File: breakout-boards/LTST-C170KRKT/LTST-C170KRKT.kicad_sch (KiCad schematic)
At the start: 0 parts

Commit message: feat: add red LED breakout board
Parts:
- added J1, J2: Conn_01x12, Connector_PinSocket_2.54mm:PinSocket_1x12_P2.54mm_Vertical, symbol Connector_Generic:Conn_01x12
- added LED1, LED10, LED11, LED12, LED2, LED3, LED4, LED5, LED6, LED7, LED8, LED9: LTST-C170KRKT, LEDC2012X120N, symbol FixedWing:LTST-C170KRKT
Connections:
- new net: J1.10 (Pin_10), LED3.1 (K)
- new net: J2.10 (Pin_10), LED3.2 (A)
- new net: J1.7 (Pin_7), LED6.1 (K)
- new net: J2.7 (Pin_7), LED6.2 (A)
- new net: J1.4 (Pin_4), LED9.1 (K)
- new net: J2.4 (Pin_4), LED9.2 (A)
- new net: J1.1 (Pin_1), LED12.1 (K)
- new net: J2.1 (Pin_1), LED12.2 (A)
- new net: J1.9 (Pin_9), LED4.1 (K)
- new net: J2.9 (Pin_9), LED4.2 (A)
- new net: J1.11 (Pin_11), LED2.1 (K)
- new net: J1.12 (Pin_12), LED1.1 (K)
- new net: J1.2 (Pin_2), LED11.1 (K)
- new net: J1.3 (Pin_3), LED10.1 (K)
- new net: J1.5 (Pin_5), LED8.1 (K)
- new net: J1.6 (Pin_6), LED7.1 (K)
- new net: J1.8 (Pin_8), LED5.1 (K)
- new net: J2.12 (Pin_12), LED1.2 (A)
- new net: J2.8 (Pin_8), LED5.2 (A)
- new net: J2.11 (Pin_11), LED2.2 (A)
- new net: J2.2 (Pin_2), LED11.2 (A)
- new net: J2.3 (Pin_3), LED10.2 (A)
- new net: J2.5 (Pin_5), LED8.2 (A)
- new net: J2.6 (Pin_6), LED7.2 (A)

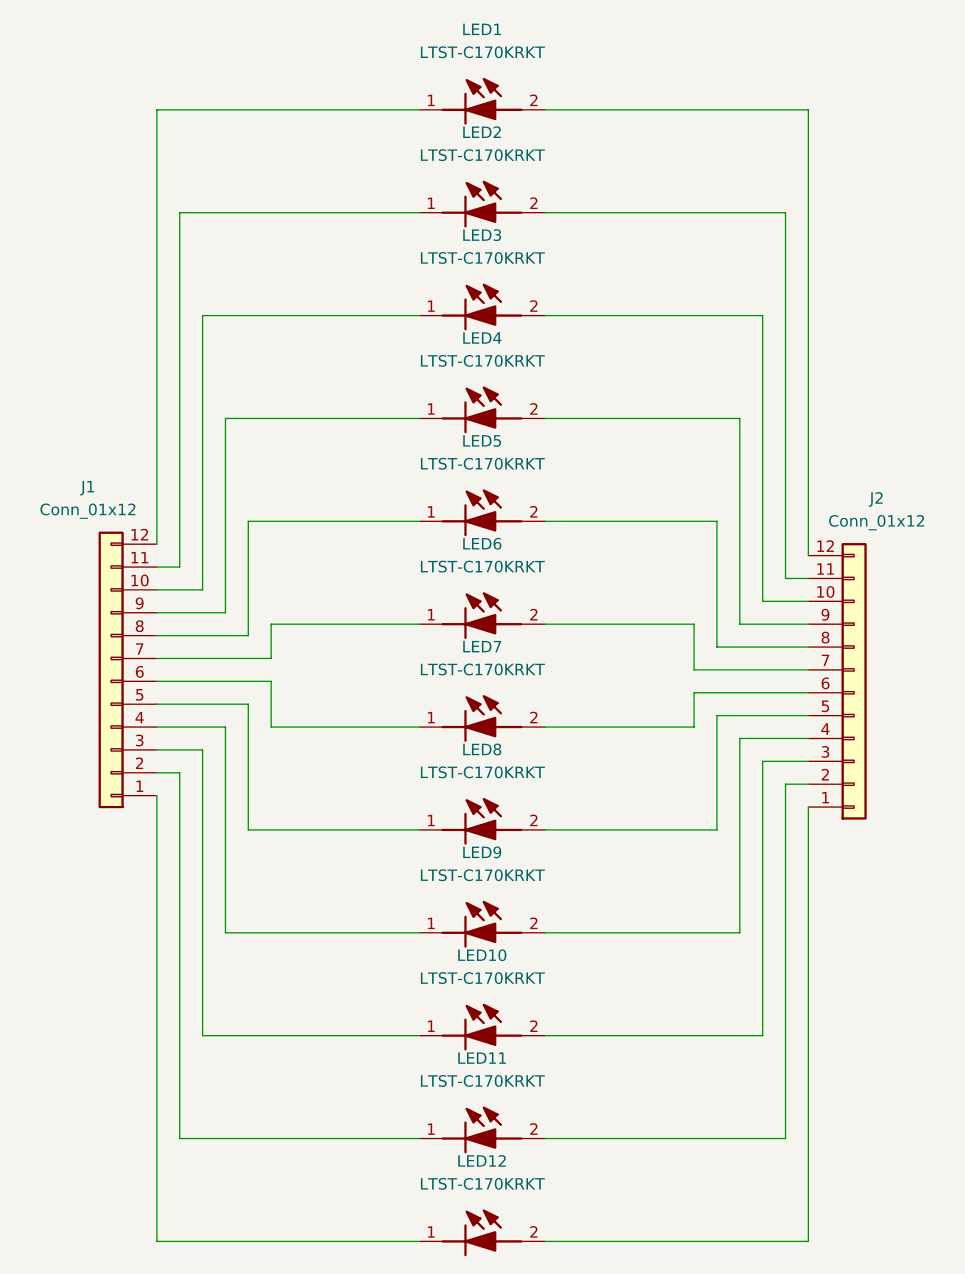
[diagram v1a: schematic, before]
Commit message: feat: create footprint for LED breakout board
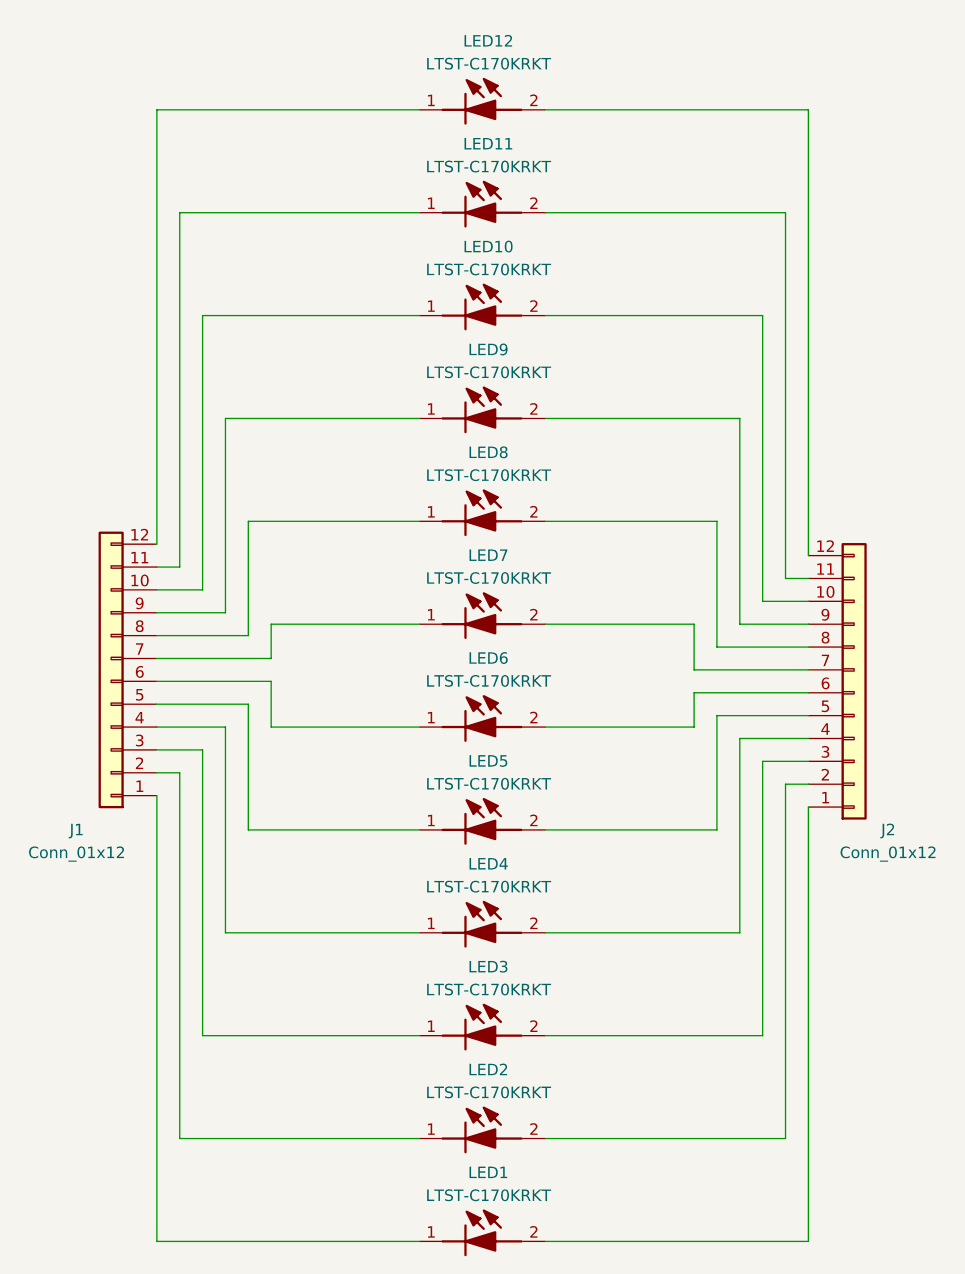
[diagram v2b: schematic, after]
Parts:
- renumbered LED12 to LED1, LED3 to LED10, LED2 to LED11, LED1 to LED12, LED11 to LED2, LED10 to LED3, LED9 to LED4, LED8 to LED5, LED7 to LED6, LED6 to LED7, LED5 to LED8, LED4 to LED9
